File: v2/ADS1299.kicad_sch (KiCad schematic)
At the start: 37 parts, among them CN1 W2A41C681KAT2A, CN2 W2A41C681KAT2A, CN3 W2A41C681KAT2A, CN4 W2A41C681KAT2A, U1 ADS1299IPAGR, U3 TPD4E1B06DCKR, U4 TPD4E1B06DCKR, U9 TPD4E1B06DCKR

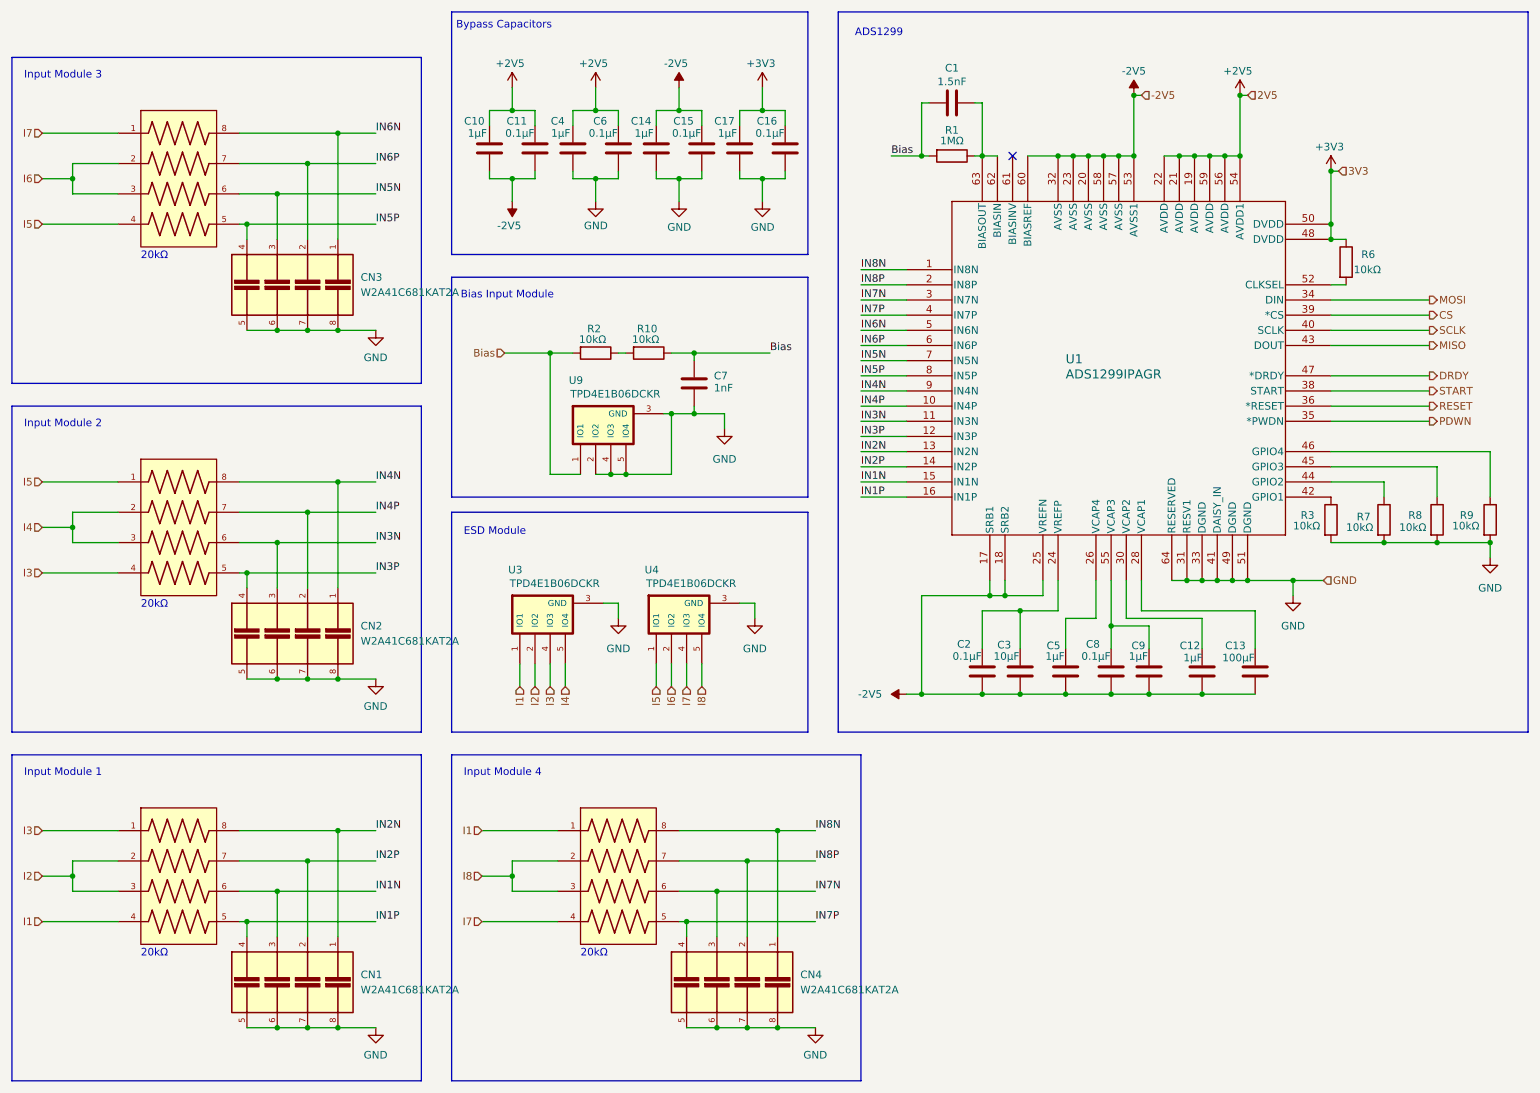
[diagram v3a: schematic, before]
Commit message: v2 volt regs and grounding
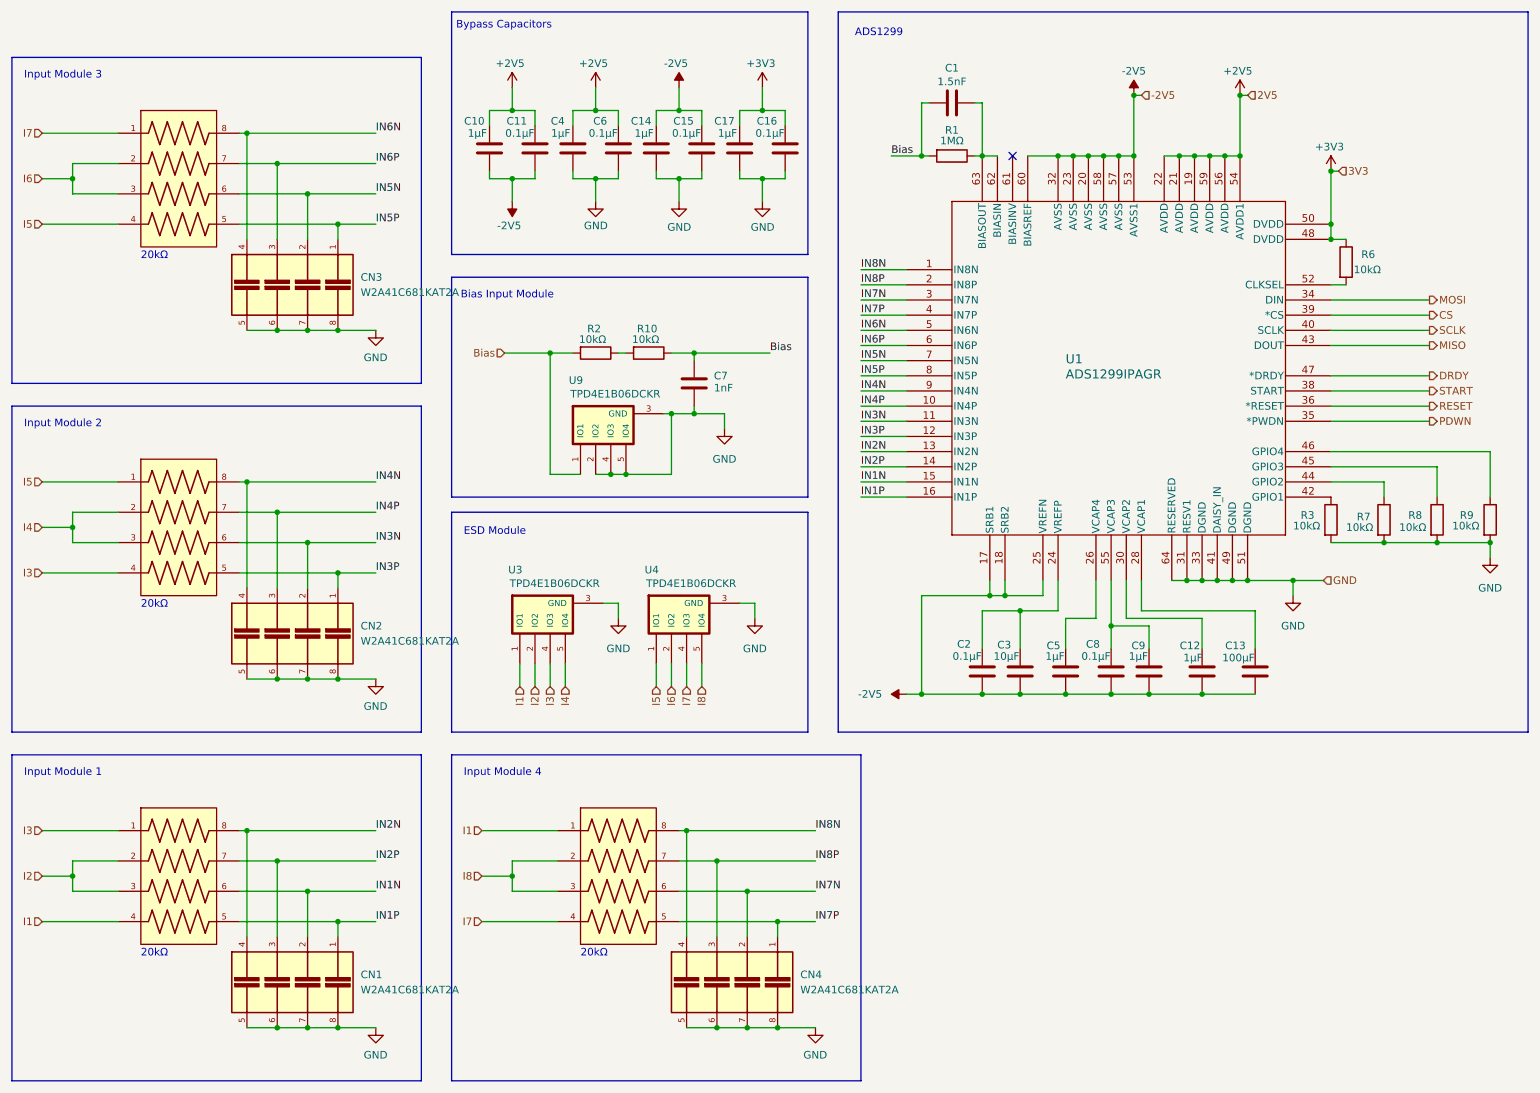
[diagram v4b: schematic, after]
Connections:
- net IN1N: now also CN1.2; no longer CN1.3
- net IN1P: now also CN1.1; no longer CN1.4
- net IN2N: now also CN1.4; no longer CN1.1
- net IN2P: now also CN1.3; no longer CN1.2
- net IN3N: now also CN2.2; no longer CN2.3
- net IN3P: now also CN2.1; no longer CN2.4
- net IN4N: now also CN2.4; no longer CN2.1
- net IN4P: now also CN2.3; no longer CN2.2
- net IN5N: now also CN3.2; no longer CN3.3
- net IN5P: now also CN3.1; no longer CN3.4
- net IN6N: now also CN3.4; no longer CN3.1
- net IN6P: now also CN3.3; no longer CN3.2
- net IN7N: now also CN4.2; no longer CN4.3
- net IN7P: now also CN4.1; no longer CN4.4
- net IN8N: now also CN4.4; no longer CN4.1
- net IN8P: now also CN4.3; no longer CN4.2

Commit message: test pins
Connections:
- net Bias: no longer R2.2, U9.1 (IO1)
- new net BI: R2.2, U9.1 (IO1)
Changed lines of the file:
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@@
 		)
 	)
-	(hierarchical_label "Bias"
+	(hierarchical_label "BI"
 		(shape input)
 		(at 100.33 71.12 180)

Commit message: v2 code
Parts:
- C10, C12, C14, C17, C4, C5, C9: value 1µF -> 1µF
- C11, C15, C16, C2, C6, C8: value 0.1µF -> 0.1µF
- C13: value 100µF -> 100µF
- C3: value 10µF -> 10µF
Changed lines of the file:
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@@
 			)
 		)
-		(property "Value" "0.1µF "
+		(property "Value" "0.1µF"
 			(at 177.8 121.92 0)
 			(effects
@@
 			)
 		)
-		(property "Value" "100µF "
+		(property "Value" "100µF"
 			(at 223.266 122.174 0)
 			(effects
@@
 			)
 		)
-		(property "Value" "0.1µF "
+		(property "Value" "0.1µF"
 			(at 199.39 121.92 0)
 			(effects
@@
 		(on_board yes)
 		(dnp no)
-		(fields_autoplaced yes)
 		(property "Reference" "CN3"
 			(at 76.2 58.4199 90)
@@
 		)
 		(property "Value" "W2A41C681KAT2A"
-			(at 76.2 60.9599 90)
+			(at 76.2 60.452 90)
 			(effects
 				(font
@@
 			)
 		)
-		(property "Value" "0.1µF "
+		(property "Value" "0.1µF"
 			(at 130.81 34.29 0)
 			(effects
@@
 			)
 		)
-		(property "Value" "1µF "
+		(property "Value" "1µF"
 			(at 95.758 34.29 0)
 			(effects
@@
 			)
 		)
-		(property "Value" "1µF "
+		(property "Value" "1µF"
 			(at 206.502 121.92 0)
 			(effects
@@
 			)
 		)
-		(property "Value" "1µF "
+		(property "Value" "1µF"
 			(at 109.728 34.29 0)
 			(effects
@@
 			)
 		)
-		(property "Value" "1µF "
+		(property "Value" "1µF"
 			(at 215.646 122.174 0)
 			(effects
@@
 			)
 		)
-		(property "Value" "10µF "
+		(property "Value" "10µF"
 			(at 184.404 121.92 0)
 			(effects
@@
 			)
 		)
-		(property "Value" "0.1µF "
+		(property "Value" "0.1µF"
 			(at 116.84 34.29 0)
 			(effects
@@
 			)
 		)
-		(property "Value" "0.1µF "
+		(property "Value" "0.1µF"
 			(at 102.87 34.29 0)
 			(effects
@@
 			)
 		)
-		(property "Value" "1µF "
+		(property "Value" "1µF"
 			(at 137.668 34.29 0)
 			(effects
@@
 			)
 		)
-		(property "Value" "0.1µF "
+		(property "Value" "0.1µF"
 			(at 144.78 34.29 0)
 			(effects
@@
 			)
 		)
-		(property "Value" "1µF "
+		(property "Value" "1µF"
 			(at 123.698 34.29 0)
 			(effects
@@
 			)
 		)
-		(property "Value" "1µF "
+		(property "Value" "1µF"
 			(at 192.532 121.92 0)
 			(effects
